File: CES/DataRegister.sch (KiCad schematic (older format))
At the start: 8 parts

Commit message: Adding 74HC versions of 74LS chips
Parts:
- removed U?: RD1, symbol 74xx:74LS173
- removed U?: RD2, symbol 74xx:74LS173
- removed U?: RD3, symbol 74xx:74LS173
- removed U?: RD4, symbol 74xx:74LS173
- added U?: RD1, symbol CES:74HC173
- added U?: RD2, symbol CES:74HC173
- added U?: RD3, symbol CES:74HC173
- added U?: RD4, symbol CES:74HC173
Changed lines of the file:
@@
 Comment4 ""
 $EndDescr
-$Comp
-L 74xx:74LS173 U?
-U 1 1 61BF54A4
-P 4150 1650
-F 0 "U?" H 4400 2400 50  0000 C CNN
-F 1 "RD1" H 4150 1650 50  0000 C CNN
-F 2 "" H 4150 1650 50  0001 C CNN
-F 3 "http://www.ti.com/lit/gpn/sn74LS173" H 4150 1650 50  0001 C CNN
-	1    4150 1650
-	1    0    0    -1
-$EndComp
-$Comp
-L 74xx:74LS173 U?
-U 1 1 61BF54AA
-P 4150 4000
-F 0 "U?" H 4400 4750 50  0000 C CNN
-F 1 "RD2" H 4150 4000 50  0000 C CNN
-F 2 "" H 4150 4000 50  0001 C CNN
-F 3 "http://www.ti.com/lit/gpn/sn74LS173" H 4150 4000 50  0001 C CNN
-	1    4150 4000
-	1    0    0    -1
-$EndComp
-$Comp
-L 74xx:74LS173 U?
-U 1 1 61BF54B0
-P 4150 6350
-F 0 "U?" H 4400 7100 50  0000 C CNN
-F 1 "RD3" H 4150 6350 50  0000 C CNN
-F 2 "" H 4150 6350 50  0001 C CNN
-F 3 "http://www.ti.com/lit/gpn/sn74LS173" H 4150 6350 50  0001 C CNN
-	1    4150 6350
-	1    0    0    -1
-$EndComp
-$Comp
-L 74xx:74LS173 U?
-U 1 1 61BF54B6
-P 4150 8700
-F 0 "U?" H 4400 9500 50  0000 C CNN
-F 1 "RD4" H 4150 8700 50  0000 C CNN
-F 2 "" H 4150 8700 50  0001 C CNN
-F 3 "http://www.ti.com/lit/gpn/sn74LS173" H 4150 8700 50  0001 C CNN
-	1    4150 8700
-	1    0    0    -1
-$EndComp
 Wire Wire Line
 	4650 1050 5850 1050
@@
 Wire Wire Line
 	1500 10400 1350 10400
+$Comp
+L CES:74HC173 U?
+U 1 1 60908DFE
+P 4150 1650
+F 0 "U?" H 4400 2400 50  0000 C CNN
+F 1 "RD1" H 4150 1650 50  0000 C CNN
+F 2 "" H 4150 1650 50  0001 C CNN
+F 3 "http://www.ti.com/lit/gpn/cd74HC173" H 4150 1650 50  0001 C CNN
+	1    4150 1650
+	1    0    0    -1
+$EndComp
+$Comp
+L CES:74HC173 U?
+U 1 1 6090AD57
+P 4150 4000
+F 0 "U?" H 4400 4750 50  0000 C CNN
+F 1 "RD2" H 4150 4000 50  0000 C CNN
+F 2 "" H 4150 4000 50  0001 C CNN
+F 3 "http://www.ti.com/lit/gpn/cd74HC173" H 4150 4000 50  0001 C CNN
+	1    4150 4000
+	1    0    0    -1
+$EndComp
+$Comp
+L CES:74HC173 U?
+U 1 1 6090B5D9
+P 4150 6350
+F 0 "U?" H 4400 7100 50  0000 C CNN
+F 1 "RD3" H 4150 6350 50  0000 C CNN
+F 2 "" H 4150 6350 50  0001 C CNN
+F 3 "http://www.ti.com/lit/gpn/cd74HC173" H 4150 6350 50  0001 C CNN
+	1    4150 6350
+	1    0    0    -1
+$EndComp
+$Comp
+L CES:74HC173 U?
+U 1 1 6090C04C
+P 4150 8700
+F 0 "U?" H 4400 9450 50  0000 C CNN
+F 1 "RD4" H 4150 8700 50  0000 C CNN
+F 2 "" H 4150 8700 50  0001 C CNN
+F 3 "http://www.ti.com/lit/gpn/cd74HC173" H 4150 8700 50  0001 C CNN
+	1    4150 8700
+	1    0    0    -1
+$EndComp
 $EndSCHEMATC

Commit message: Control Unit
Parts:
- gave numbers to parts that had none: 8
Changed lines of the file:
@@
 $Descr A4 8268 11693 portrait
 encoding utf-8
-Sheet 6 16
+Sheet 6 17
 Title "CES"
 Date "2021-04-24"
@@
 ESA15
 $Comp
-L power:VCC #PWR?
+L power:VCC #PWR0613
 U 1 1 609F118D
 P 4150 7800
-F 0 "#PWR?" H 4150 7650 50  0001 C CNN
+F 0 "#PWR0613" H 4150 7650 50  0001 C CNN
 F 1 "VCC" H 4165 7973 50  0000 C CNN
 F 2 "" H 4150 7800 50  0001 C CNN
@@
 $EndComp
 $Comp
-L power:VCC #PWR?
+L power:VCC #PWR0611
 U 1 1 609F1717
 P 4150 5450
-F 0 "#PWR?" H 4150 5300 50  0001 C CNN
+F 0 "#PWR0611" H 4150 5300 50  0001 C CNN
 F 1 "VCC" H 4165 5623 50  0000 C CNN
 F 2 "" H 4150 5450 50  0001 C CNN
@@
 $EndComp
 $Comp
-L power:VCC #PWR?
+L power:VCC #PWR0609
 U 1 1 609F1CAB
 P 4150 3100
-F 0 "#PWR?" H 4150 2950 50  0001 C CNN
+F 0 "#PWR0609" H 4150 2950 50  0001 C CNN
 F 1 "VCC" H 4165 3273 50  0000 C CNN
 F 2 "" H 4150 3100 50  0001 C CNN
@@
 $EndComp
 $Comp
-L power:VCC #PWR?
+L power:VCC #PWR0607
 U 1 1 609F239F
 P 4150 750
-F 0 "#PWR?" H 4150 600 50  0001 C CNN
+F 0 "#PWR0607" H 4150 600 50  0001 C CNN
 F 1 "VCC" H 4165 923 50  0000 C CNN
 F 2 "" H 4150 750 50  0001 C CNN
@@
 $EndComp
 $Comp
-L power:GND #PWR?
+L power:GND #PWR0608
 U 1 1 609F2BCB
 P 4150 2550
-F 0 "#PWR?" H 4150 2300 50  0001 C CNN
+F 0 "#PWR0608" H 4150 2300 50  0001 C CNN
 F 1 "GND" H 4155 2377 50  0000 C CNN
 F 2 "" H 4150 2550 50  0001 C CNN
@@
 $EndComp
 $Comp
-L power:GND #PWR?
+L power:GND #PWR0610
 U 1 1 609F31F5
 P 4150 4900
-F 0 "#PWR?" H 4150 4650 50  0001 C CNN
+F 0 "#PWR0610" H 4150 4650 50  0001 C CNN
 F 1 "GND" H 4155 4727 50  0000 C CNN
 F 2 "" H 4150 4900 50  0001 C CNN
@@
 $EndComp
 $Comp
-L power:GND #PWR?
+L power:GND #PWR0612
 U 1 1 609F375F
 P 4150 7250
-F 0 "#PWR?" H 4150 7000 50  0001 C CNN
+F 0 "#PWR0612" H 4150 7000 50  0001 C CNN
 F 1 "GND" H 4155 7077 50  0000 C CNN
 F 2 "" H 4150 7250 50  0001 C CNN
@@
 $EndComp
 $Comp
-L power:GND #PWR?
+L power:GND #PWR0614
 U 1 1 609F3CC7
 P 4150 9600
-F 0 "#PWR?" H 4150 9350 50  0001 C CNN
+F 0 "#PWR0614" H 4150 9350 50  0001 C CNN
 F 1 "GND" H 4155 9427 50  0000 C CNN
 F 2 "" H 4150 9600 50  0001 C CNN
@@
 Connection ~ 3400 1950
 $Comp
-L power:GND #PWR?
+L power:GND #PWR0603
 U 1 1 609F88E0
 P 3400 2350
-F 0 "#PWR?" H 3400 2100 50  0001 C CNN
+F 0 "#PWR0603" H 3400 2100 50  0001 C CNN
 F 1 "GND" H 3405 2177 50  0000 C CNN
 F 2 "" H 3400 2350 50  0001 C CNN
@@
 Connection ~ 3400 4300
 $Comp
-L power:GND #PWR?
+L power:GND #PWR0604
 U 1 1 609F9981
 P 3400 4700
-F 0 "#PWR?" H 3400 4450 50  0001 C CNN
+F 0 "#PWR0604" H 3400 4450 50  0001 C CNN
 F 1 "GND" H 3405 4527 50  0000 C CNN
 F 2 "" H 3400 4700 50  0001 C CNN
@@
 Connection ~ 3400 6650
 $Comp
-L power:GND #PWR?
+L power:GND #PWR0605
 U 1 1 609FA6DD
 P 3400 7050
-F 0 "#PWR?" H 3400 6800 50  0001 C CNN
+F 0 "#PWR0605" H 3400 6800 50  0001 C CNN
 F 1 "GND" H 3405 6877 50  0000 C CNN
 F 2 "" H 3400 7050 50  0001 C CNN
@@
 Connection ~ 3400 9000
 $Comp
-L power:GND #PWR?
+L power:GND #PWR0606
 U 1 1 609FB6BB
 P 3400 9400
-F 0 "#PWR?" H 3400 9150 50  0001 C CNN
+F 0 "#PWR0606" H 3400 9150 50  0001 C CNN
 F 1 "GND" H 3405 9227 50  0000 C CNN
 F 2 "" H 3400 9400 50  0001 C CNN
@@
 P 1050 10650
 AR Path="/60832B49/61BE6B6E/60A10FA6" Ref="C?"  Part="1"
-AR Path="/60832B49/61BE8441/60A10FA6" Ref="C?"  Part="1"
-F 0 "C?" H 1100 10750 50  0000 L CNN
+AR Path="/60832B49/61BE8441/60A10FA6" Ref="C601"  Part="1"
+F 0 "C601" H 1100 10750 50  0000 L CNN
 F 1 "100nF" H 1100 10550 50  0000 L CNN
 F 2 "" H 1088 10500 50  0001 C CNN
@@
 P 1350 10650
 AR Path="/60832B49/61BE6B6E/60A10FAC" Ref="C?"  Part="1"
-AR Path="/60832B49/61BE8441/60A10FAC" Ref="C?"  Part="1"
-F 0 "C?" H 1400 10750 50  0000 L CNN
+AR Path="/60832B49/61BE8441/60A10FAC" Ref="C602"  Part="1"
+F 0 "C602" H 1400 10750 50  0000 L CNN
 F 1 "100nF" H 1400 10550 50  0000 L CNN
 F 2 "" H 1388 10500 50  0001 C CNN
@@
 P 1650 10650
 AR Path="/60832B49/61BE6B6E/60A10FB2" Ref="C?"  Part="1"
-AR Path="/60832B49/61BE8441/60A10FB2" Ref="C?"  Part="1"
-F 0 "C?" H 1700 10750 50  0000 L CNN
+AR Path="/60832B49/61BE8441/60A10FB2" Ref="C603"  Part="1"
+F 0 "C603" H 1700 10750 50  0000 L CNN
 F 1 "100nF" H 1700 10550 50  0000 L CNN
 F 2 "" H 1688 10500 50  0001 C CNN
@@
 P 1950 10650
 AR Path="/60832B49/61BE6B6E/60A10FB8" Ref="C?"  Part="1"
-AR Path="/60832B49/61BE8441/60A10FB8" Ref="C?"  Part="1"
-F 0 "C?" H 2000 10750 50  0000 L CNN
+AR Path="/60832B49/61BE8441/60A10FB8" Ref="C604"  Part="1"
+F 0 "C604" H 2000 10750 50  0000 L CNN
 F 1 "100nF" H 2000 10550 50  0000 L CNN
 F 2 "" H 1988 10500 50  0001 C CNN
@@
 P 1500 10900
 AR Path="/60832B49/61BE6B6E/60A10FD0" Ref="#PWR?"  Part="1"
-AR Path="/60832B49/61BE8441/60A10FD0" Ref="#PWR?"  Part="1"
-F 0 "#PWR?" H 1500 10650 50  0001 C CNN
+AR Path="/60832B49/61BE8441/60A10FD0" Ref="#PWR0602"  Part="1"
+F 0 "#PWR0602" H 1500 10650 50  0001 C CNN
 F 1 "GND" H 1505 10727 50  0000 C CNN
 F 2 "" H 1500 10900 50  0001 C CNN
@@
 P 1500 10400
 AR Path="/60832B49/61BE6B6E/60A10FD8" Ref="#PWR?"  Part="1"
-AR Path="/60832B49/61BE8441/60A10FD8" Ref="#PWR?"  Part="1"
-F 0 "#PWR?" H 1500 10250 50  0001 C CNN
+AR Path="/60832B49/61BE8441/60A10FD8" Ref="#PWR0601"  Part="1"
+F 0 "#PWR0601" H 1500 10250 50  0001 C CNN
 F 1 "VCC" H 1515 10573 50  0000 C CNN
 F 2 "" H 1500 10400 50  0001 C CNN
@@
 	1500 10400 1350 10400
 $Comp
-L CES:74HC173 U?
+L CES:74HC173 U601
 U 1 1 60908DFE
 P 4150 1650
-F 0 "U?" H 4400 2400 50  0000 C CNN
+F 0 "U601" H 4400 2400 50  0000 C CNN
 F 1 "RD1" H 4150 1650 50  0000 C CNN
 F 2 "" H 4150 1650 50  0001 C CNN
@@
 $EndComp
 $Comp
-L CES:74HC173 U?
+L CES:74HC173 U602
 U 1 1 6090AD57
 P 4150 4000
-F 0 "U?" H 4400 4750 50  0000 C CNN
+F 0 "U602" H 4400 4750 50  0000 C CNN
 F 1 "RD2" H 4150 4000 50  0000 C CNN
 F 2 "" H 4150 4000 50  0001 C CNN
@@
 $EndComp
 $Comp
-L CES:74HC173 U?
+L CES:74HC173 U603
 U 1 1 6090B5D9
 P 4150 6350
-F 0 "U?" H 4400 7100 50  0000 C CNN
+F 0 "U603" H 4400 7100 50  0000 C CNN
 F 1 "RD3" H 4150 6350 50  0000 C CNN
 F 2 "" H 4150 6350 50  0001 C CNN
@@
 $EndComp
 $Comp
-L CES:74HC173 U?
+L CES:74HC173 U604
 U 1 1 6090C04C
 P 4150 8700
-F 0 "U?" H 4400 9450 50  0000 C CNN
+F 0 "U604" H 4400 9450 50  0000 C CNN
 F 1 "RD4" H 4150 8700 50  0000 C CNN
 F 2 "" H 4150 8700 50  0001 C CNN

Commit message: Assigning footprints and generating netlist
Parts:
- C601, C602, C603, C604: footprint (none) -> Capacitor_THT:CP_Radial_D5.0mm_P2.50mm
- U601, U602, U603, U604: footprint (none) -> Package_DIP:DIP-16_W7.62mm
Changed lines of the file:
@@
 F 0 "C601" H 1100 10750 50  0000 L CNN
 F 1 "100nF" H 1100 10550 50  0000 L CNN
-F 2 "" H 1088 10500 50  0001 C CNN
+F 2 "Capacitor_THT:CP_Radial_D5.0mm_P2.50mm" H 1088 10500 50  0001 C CNN
 F 3 "~" H 1050 10650 50  0001 C CNN
 	1    1050 10650
@@
 F 0 "C602" H 1400 10750 50  0000 L CNN
 F 1 "100nF" H 1400 10550 50  0000 L CNN
-F 2 "" H 1388 10500 50  0001 C CNN
+F 2 "Capacitor_THT:CP_Radial_D5.0mm_P2.50mm" H 1388 10500 50  0001 C CNN
 F 3 "~" H 1350 10650 50  0001 C CNN
 	1    1350 10650
@@
 F 0 "C603" H 1700 10750 50  0000 L CNN
 F 1 "100nF" H 1700 10550 50  0000 L CNN
-F 2 "" H 1688 10500 50  0001 C CNN
+F 2 "Capacitor_THT:CP_Radial_D5.0mm_P2.50mm" H 1688 10500 50  0001 C CNN
 F 3 "~" H 1650 10650 50  0001 C CNN
 	1    1650 10650
@@
 F 0 "C604" H 2000 10750 50  0000 L CNN
 F 1 "100nF" H 2000 10550 50  0000 L CNN
-F 2 "" H 1988 10500 50  0001 C CNN
+F 2 "Capacitor_THT:CP_Radial_D5.0mm_P2.50mm" H 1988 10500 50  0001 C CNN
 F 3 "~" H 1950 10650 50  0001 C CNN
 	1    1950 10650
@@
 F 0 "U601" H 4400 2400 50  0000 C CNN
 F 1 "RD1" H 4150 1650 50  0000 C CNN
-F 2 "" H 4150 1650 50  0001 C CNN
+F 2 "Package_DIP:DIP-16_W7.62mm" H 4150 1650 50  0001 C CNN
 F 3 "http://www.ti.com/lit/gpn/cd74HC173" H 4150 1650 50  0001 C CNN
 	1    4150 1650
@@
 F 0 "U602" H 4400 4750 50  0000 C CNN
 F 1 "RD2" H 4150 4000 50  0000 C CNN
-F 2 "" H 4150 4000 50  0001 C CNN
+F 2 "Package_DIP:DIP-16_W7.62mm" H 4150 4000 50  0001 C CNN
 F 3 "http://www.ti.com/lit/gpn/cd74HC173" H 4150 4000 50  0001 C CNN
 	1    4150 4000
@@
 F 0 "U603" H 4400 7100 50  0000 C CNN
 F 1 "RD3" H 4150 6350 50  0000 C CNN
-F 2 "" H 4150 6350 50  0001 C CNN
+F 2 "Package_DIP:DIP-16_W7.62mm" H 4150 6350 50  0001 C CNN
 F 3 "http://www.ti.com/lit/gpn/cd74HC173" H 4150 6350 50  0001 C CNN
 	1    4150 6350
@@
 F 0 "U604" H 4400 9450 50  0000 C CNN
 F 1 "RD4" H 4150 8700 50  0000 C CNN
-F 2 "" H 4150 8700 50  0001 C CNN
+F 2 "Package_DIP:DIP-16_W7.62mm" H 4150 8700 50  0001 C CNN
 F 3 "http://www.ti.com/lit/gpn/cd74HC173" H 4150 8700 50  0001 C CNN
 	1    4150 8700

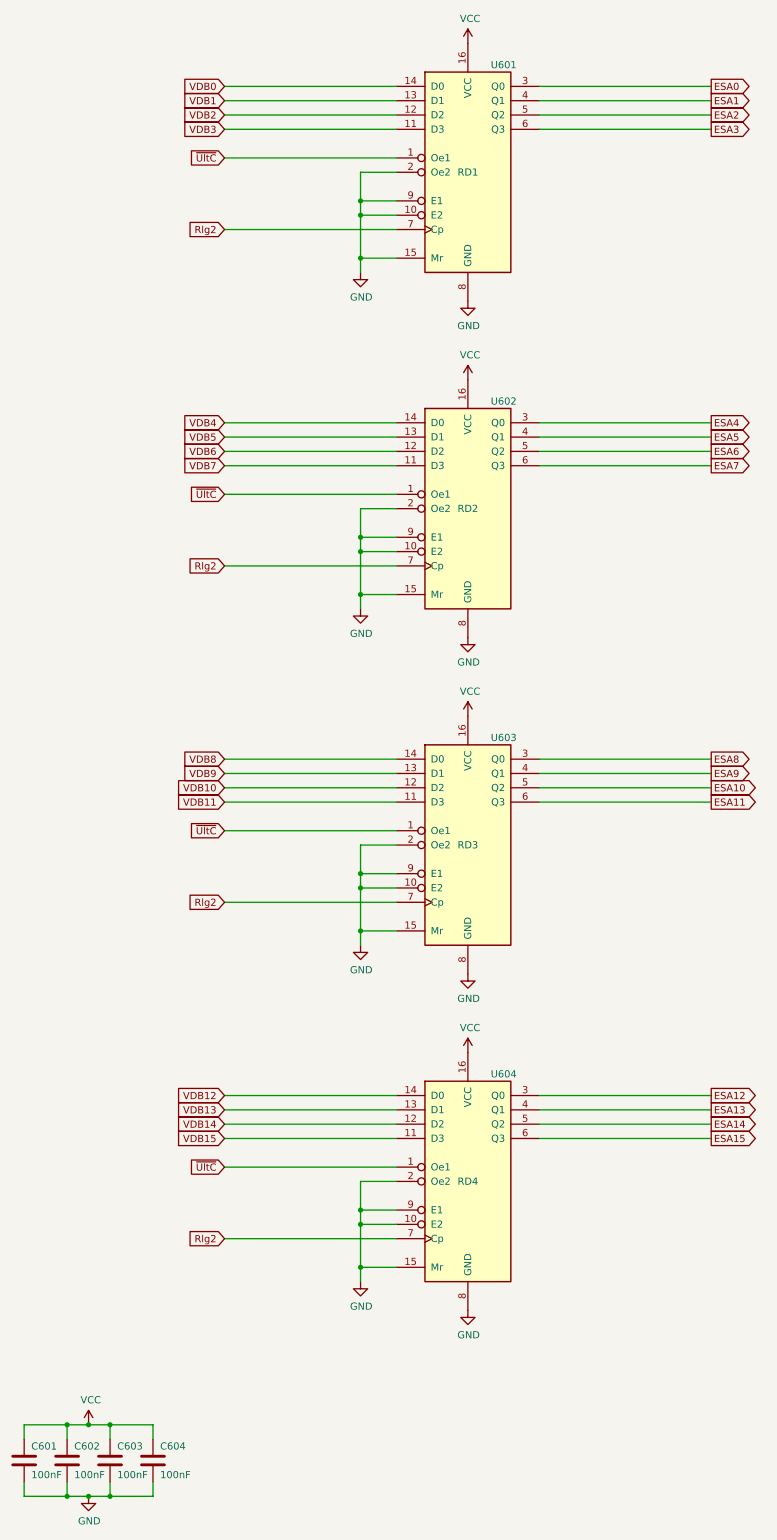
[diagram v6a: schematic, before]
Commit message: Correcting footprints errors
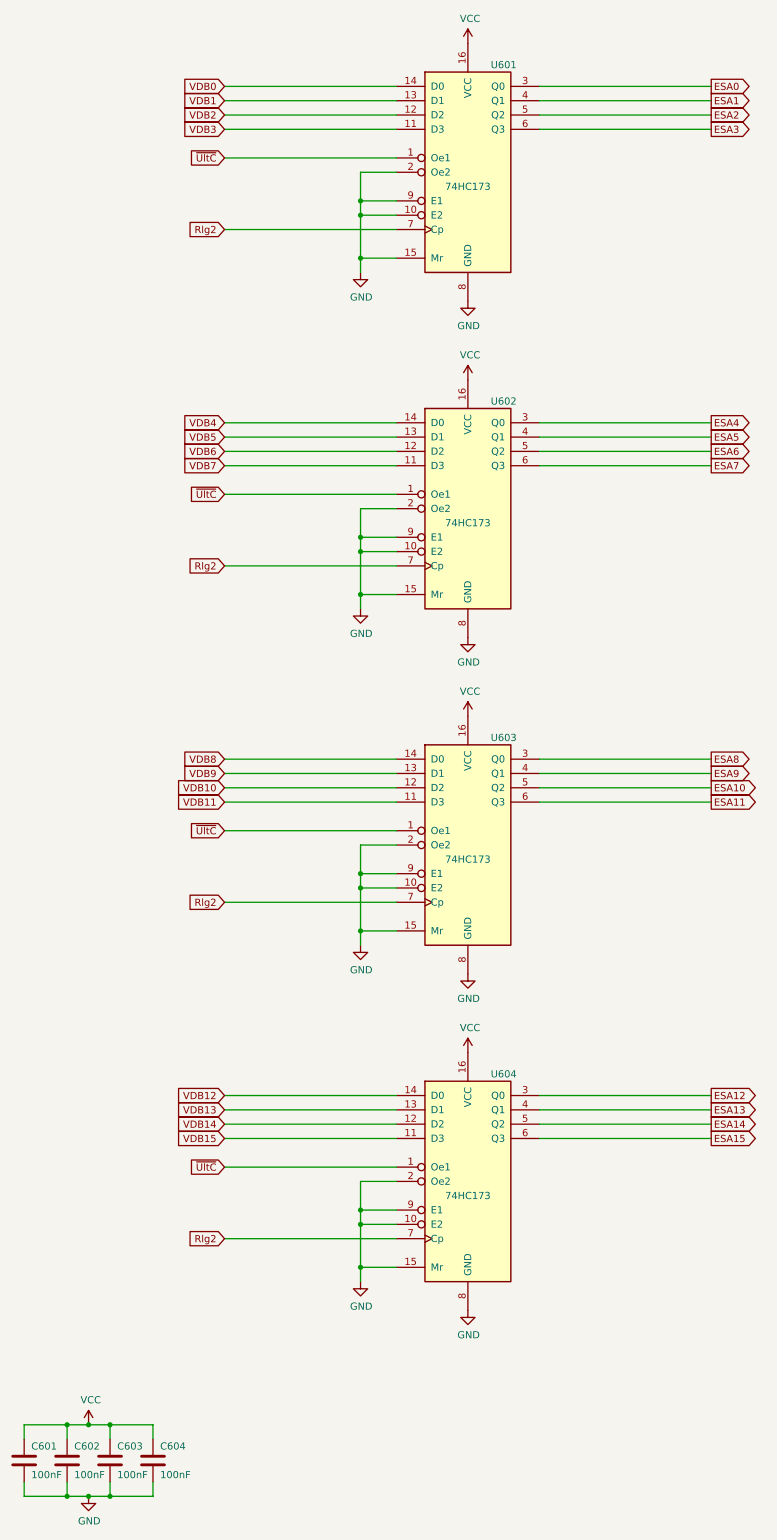
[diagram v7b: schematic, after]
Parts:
- C601, C602, C603, C604: footprint Capacitor_THT:CP_Radial_D5.0mm_P2.50mm -> Capacitor_THT:C_Disc_D4.3mm_W1.9mm_P5.00mm
- U601: value RD1 -> 74HC173
- U602: value RD2 -> 74HC173
- U603: value RD3 -> 74HC173
- U604: value RD4 -> 74HC173
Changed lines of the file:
@@
 F 0 "C601" H 1100 10750 50  0000 L CNN
 F 1 "100nF" H 1100 10550 50  0000 L CNN
-F 2 "Capacitor_THT:CP_Radial_D5.0mm_P2.50mm" H 1088 10500 50  0001 C CNN
+F 2 "Capacitor_THT:C_Disc_D4.3mm_W1.9mm_P5.00mm" H 1088 10500 50  0001 C CNN
 F 3 "~" H 1050 10650 50  0001 C CNN
 	1    1050 10650
@@
 F 0 "C602" H 1400 10750 50  0000 L CNN
 F 1 "100nF" H 1400 10550 50  0000 L CNN
-F 2 "Capacitor_THT:CP_Radial_D5.0mm_P2.50mm" H 1388 10500 50  0001 C CNN
+F 2 "Capacitor_THT:C_Disc_D4.3mm_W1.9mm_P5.00mm" H 1388 10500 50  0001 C CNN
 F 3 "~" H 1350 10650 50  0001 C CNN
 	1    1350 10650
@@
 F 0 "C603" H 1700 10750 50  0000 L CNN
 F 1 "100nF" H 1700 10550 50  0000 L CNN
-F 2 "Capacitor_THT:CP_Radial_D5.0mm_P2.50mm" H 1688 10500 50  0001 C CNN
+F 2 "Capacitor_THT:C_Disc_D4.3mm_W1.9mm_P5.00mm" H 1688 10500 50  0001 C CNN
 F 3 "~" H 1650 10650 50  0001 C CNN
 	1    1650 10650
@@
 F 0 "C604" H 2000 10750 50  0000 L CNN
 F 1 "100nF" H 2000 10550 50  0000 L CNN
-F 2 "Capacitor_THT:CP_Radial_D5.0mm_P2.50mm" H 1988 10500 50  0001 C CNN
+F 2 "Capacitor_THT:C_Disc_D4.3mm_W1.9mm_P5.00mm" H 1988 10500 50  0001 C CNN
 F 3 "~" H 1950 10650 50  0001 C CNN
 	1    1950 10650
@@
 P 4150 1650
 F 0 "U601" H 4400 2400 50  0000 C CNN
-F 1 "RD1" H 4150 1650 50  0000 C CNN
+F 1 "74HC173" H 4150 1550 50  0000 C CNN
 F 2 "Package_DIP:DIP-16_W7.62mm" H 4150 1650 50  0001 C CNN
 F 3 "http://www.ti.com/lit/gpn/cd74HC173" H 4150 1650 50  0001 C CNN
@@
 P 4150 4000
 F 0 "U602" H 4400 4750 50  0000 C CNN
-F 1 "RD2" H 4150 4000 50  0000 C CNN
+F 1 "74HC173" H 4150 3900 50  0000 C CNN
 F 2 "Package_DIP:DIP-16_W7.62mm" H 4150 4000 50  0001 C CNN
 F 3 "http://www.ti.com/lit/gpn/cd74HC173" H 4150 4000 50  0001 C CNN
@@
 P 4150 6350
 F 0 "U603" H 4400 7100 50  0000 C CNN
-F 1 "RD3" H 4150 6350 50  0000 C CNN
+F 1 "74HC173" H 4150 6250 50  0000 C CNN
 F 2 "Package_DIP:DIP-16_W7.62mm" H 4150 6350 50  0001 C CNN
 F 3 "http://www.ti.com/lit/gpn/cd74HC173" H 4150 6350 50  0001 C CNN
@@
 P 4150 8700
 F 0 "U604" H 4400 9450 50  0000 C CNN
-F 1 "RD4" H 4150 8700 50  0000 C CNN
+F 1 "74HC173" H 4150 8600 50  0000 C CNN
 F 2 "Package_DIP:DIP-16_W7.62mm" H 4150 8700 50  0001 C CNN
 F 3 "http://www.ti.com/lit/gpn/cd74HC173" H 4150 8700 50  0001 C CNN
